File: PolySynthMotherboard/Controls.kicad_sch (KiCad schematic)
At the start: 92 parts, among them SW601 ENV1_B, SW602 ENV2_B, SW603 LFO1_B, SW604 LFO2_B, SW605 LFO3_B, SW606 MIX1_B, SW607 MIX2_B, SW608 MENU_B, SW609 FF_B, SW610 HP_B, SW611 HP_B, U204 ILI9341, U501 MCP23S17_SS

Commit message: board layout
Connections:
- net ENCA_L: now also U501.2 (GPB1); no longer U501.1 (GPB0)
- net ENCA_R: now also U501.1 (GPB0); no longer U501.2 (GPB1)
- net ENCB_L: now also U501.4 (GPB3); no longer U501.3 (GPB2)
- net ENCB_R: now also U501.3 (GPB2); no longer U501.4 (GPB3)
- net ENCC_L: now also U501.6 (GPB5); no longer U501.5 (GPB4), U501.7 (GPB6)
- net ENCC_R: now also U501.5 (GPB4); no longer U501.6 (GPB5), U501.8 (GPB7)
- net ENCD_L: now also U501.8 (GPB7)
- net ENCD_R: now also U501.7 (GPB6)
- net ENV1_B: now also U501.28 (GPA7); no longer U501.21 (GPA0)
- net ENV2_B: now also U501.27 (GPA6); no longer U501.22 (GPA1)
- net LFO1_B: now also U501.26 (GPA5); no longer U501.23 (GPA2)
- net LFO2_B: now also U501.25 (GPA4); no longer U501.24 (GPA3)
- net LFO3_B: now also U501.24 (GPA3); no longer U501.25 (GPA4)
- net MENU_B: now also U501.21 (GPA0); no longer U501.28 (GPA7)
- net MIX1_B: now also U501.23 (GPA2); no longer U501.26 (GPA5)
- net MIX2_B: now also U501.22 (GPA1); no longer U501.27 (GPA6)
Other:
- moved on the sheet: R625, R626, SW609, SW610

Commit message: new voice board proj
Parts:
- RE606: value ENC_RES -> ENC_LES
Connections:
- net ENCA_L: now also C217.1, R601.2, RE601.A, U501.1 (GPB0); no longer C217.1, R602.2, RE601.B, U501.2 (GPB1)
- net ENCA_R: now also C217.1, R602.2, RE601.B, U501.2 (GPB1); no longer C217.1, R601.2, RE601.A, U501.1 (GPB0)
- net ENCB_L: now also C217.1, R605.2, RE602.A, U501.3 (GPB2); no longer C217.1, R606.2, RE602.B, U501.4 (GPB3)
- net ENCB_R: now also C217.1, R606.2, RE602.B, U501.4 (GPB3); no longer C217.1, R605.2, RE602.A, U501.3 (GPB2)
- net ENCCF_L: now also C217.1, R617.2, RE605.A, U501.28 (GPA7); no longer C217.1, R618.2, RE605.B, U501.21 (GPA0)
- net ENCCF_R: now also C217.1, R618.2, RE605.B, U501.27 (GPA6); no longer C217.1, R617.2, RE605.A, U501.22 (GPA1)
- net ENCC_L: now also C217.1, R608.2, RE603.A, U501.5 (GPB4); no longer C217.1, R609.2, RE603.B, U501.6 (GPB5)
- net ENCC_R: now also C217.1, R609.2, RE603.B, U501.6 (GPB5); no longer C217.1, R608.2, RE603.A, U501.5 (GPB4)
- net ENCDEPTH_L: now also C217.1, R627.2, RE609.A, U501.8 (GPB7); no longer C217.1, R628.2, RE609.B, U501.7 (GPB6)
- net ENCDEPTH_R: now also C217.1, R628.2, RE609.B, U501.7 (GPB6); no longer C217.1, R627.2, RE609.A, U501.8 (GPB7)
- net ENCD_L: now also C217.1, R611.2, RE604.A, U501.7 (GPB6); no longer C217.1, R612.2, RE604.B, U501.8 (GPB7)
- net ENCD_R: now also C217.1, R612.2, RE604.B, U501.8 (GPB7); no longer C217.1, R611.2, RE604.A, U501.7 (GPB6)
- net ENCFOLD_L: now also C217.1, R623.2, RE608.A, U501.22 (GPA1); no longer C217.1, R624.2, RE608.B, U501.27 (GPA6)
- net ENCFOLD_R: now also C217.1, R624.2, RE608.B, U501.21 (GPA0); no longer C217.1, R623.2, RE608.A, U501.28 (GPA7)
- net ENCPWM_L: now also C217.1, R621.2, RE607.A, U501.24 (GPA3); no longer C217.1, R622.2, RE607.B, U501.25 (GPA4)
- net ENCPWM_R: now also C217.1, R622.2, RE607.B, U501.23 (GPA2); no longer C217.1, R621.2, RE607.A, U501.26 (GPA5)
- net ENCRES_L: now also C217.1, R619.2, RE606.A, U501.26 (GPA5); no longer C217.1, R620.2, RE606.B, U501.23 (GPA2)
- net ENCRES_R: now also C217.1, R620.2, RE606.B, U501.25 (GPA4); no longer C217.1, R619.2, RE606.A, U501.24 (GPA3)
- net DISP_RST renamed DISP_LST

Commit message: fixed git maybe
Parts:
- added C217 (x2): 10n, Capacitor_SMD:C_0805_2012Metric, symbol Device:C
- added R630, R631, R632: 47k, PCM_Resistor_SMD_AKL:R_0805_2012Metric, symbol Device:R_US
- added SW612: ENC_MENU, Alps_Rotary_Encoder:RotaryEncoder_Alps_EC11E-Switch_Vertical_H20mm_5Pin, symbol Device:RotaryEncoder_Switch
- SW608: value MENU_B -> ALT_B
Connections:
- net +3.3V: now also R630.1, R631.1, R632.1
- net GND: now also C217.2, C217.2, SW612.C, SW612.S2
- net MENU_B: now also U501.1 (GPB0), R632.2, SW612.S1; no longer R616.2, SW608.2 (B), U501.21 (GPA0)
- net ENCMENU_R: now reaches U501.2 (GPB1)
- net ENCMENU_R: now also C217.1, R631.2, SW612.B
- net ENCMENU_L: now reaches U501.3 (GPB2)
- net ENCMENU_L: now also C217.1, R630.2, SW612.A
- new net ALT_B: R616.2, SW608.2 (B), U501.21 (GPA0)
- no-connect marks 5 -> 2
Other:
- moved on the sheet: C217, R616, SW608, U204

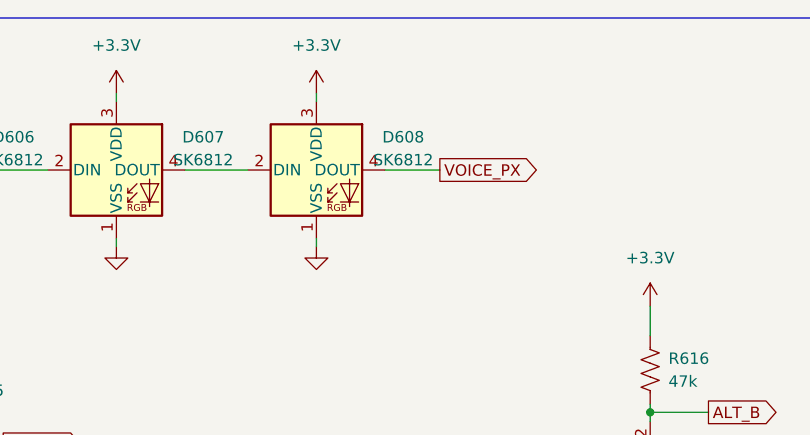
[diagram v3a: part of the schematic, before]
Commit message: cleaned up CV opamps
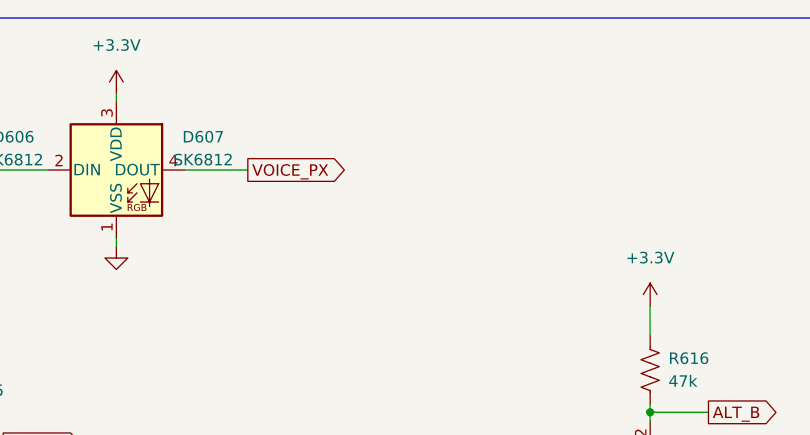
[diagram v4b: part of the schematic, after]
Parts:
- removed D608: SK6812, LED_SMD:LED_SK6812_PLCC4_5.0x5.0mm_P3.2mm, symbol LED:SK6812
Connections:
- net VOICE_PX: now also D607.4 (DOUT)
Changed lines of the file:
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@@
     (stroke (width 0) (type default))
   )
-  (wire (pts (xy 197.104 33.274) (xy 203.2 33.274))
-    (stroke (width 0) (type default))
-  )
   (wire (pts (xy 149.098 231.14) (xy 149.098 232.156))
     (stroke (width 0) (type default))
@@
     (stroke (width 0) (type default))
   )
-  (wire (pts (xy 189.484 40.894) (xy 189.484 41.783))
-    (stroke (width 0) (type default))
-  )
   (wire (pts (xy 225.679 116.332) (xy 225.679 117.602))
     (stroke (width 0) (type default))
@@
     (stroke (width 0) (type default))
   )
-  (wire (pts (xy 189.484 24.765) (xy 189.484 25.654))
-    (stroke (width 0) (type default))
-  )
   (wire (pts (xy 156.845 219.075) (xy 156.845 220.345))
     (stroke (width 0) (type default))
@@
     )
   )
-  (global_label "VOICE_PX" (shape output) (at 203.2 33.274 0) (fields_autoplaced)
+  (global_label "VOICE_PX" (shape output) (at 181.864 33.274 0) (fields_autoplaced)
     (effects (font (size 1.27 1.27)) (justify left))
-    (property "Intersheetrefs" "${INTERSHEET_REFS}" (at 215.0752 33.274 0)
+    (property "Intersheetrefs" "${INTERSHEET_REFS}" (at 193.7392 33.274 0)
       (effects (font (size 1.27 1.27)) (justify left) hide)
     )
@@
     )
   )
-  (symbol (lib_id "LED:SK6812") (at 189.484 33.274 0) (unit 1)
-    (in_bom yes) (on_board yes) (dnp no) (fields_autoplaced)
-    (property "Reference" "D608" (at 199.136 29.6261 0)
-      (effects (font (size 1.27 1.27)))
-    )
-    (property "Value" "SK6812" (at 199.136 32.1661 0)
-      (effects (font (size 1.27 1.27)))
-    )
-    (property "Footprint" "LED_SMD:LED_SK6812_PLCC4_5.0x5.0mm_P3.2mm" (at 190.754 40.894 0)
-      (effects (font (size 1.27 1.27)) (justify left top) hide)
-    )
-    (property "Datasheet" "https://cdn-shop.adafruit.com/product-files/1138/SK6812+LED+datasheet+.pdf" (at 192.024 42.799 0)
-      (effects (font (size 1.27 1.27)) (justify left top) hide)
-    )
-    (pin "1")
-    (pin "2")
-    (pin "3")
-    (pin "4")
-    (instances
-      (project "PolySynthMotherboard"
-        (path "/22649217-9810-470f-bc7b-6f743ad2b90e/f0372297-a883-4012-af0b-9ec6adb58eca"
-          (reference "D608") (unit 1)
-        )
-      )
-    )
-  )
   (symbol (lib_id "Device:C") (at 365.633 36.449 0) (unit 1)
     (in_bom yes) (on_board yes) (dnp no)
@@
     )
   )
-  (symbol (lib_id "power:+3.3V") (at 189.484 24.765 0) (unit 1)
-    (in_bom yes) (on_board yes) (dnp no) (fields_autoplaced)
-    (property "Reference" "#PWR0695" (at 189.484 28.575 0)
-      (effects (font (size 1.27 1.27)) hide)
-    )
-    (property "Value" "+3.3V" (at 189.484 19.431 0)
-      (effects (font (size 1.27 1.27)))
-    )
-    (property "Footprint" "" (at 189.484 24.765 0)
-      (effects (font (size 1.27 1.27)) hide)
-    )
-    (property "Datasheet" "" (at 189.484 24.765 0)
-      (effects (font (size 1.27 1.27)) hide)
-    )
-    (pin "1")
-    (instances
-      (project "PolySynthMotherboard"
-        (path "/22649217-9810-470f-bc7b-6f743ad2b90e/f0372297-a883-4012-af0b-9ec6adb58eca"
-          (reference "#PWR0695") (unit 1)
-        )
-      )
-    )
-  )
   (symbol (lib_id "Device:R_US") (at 180.721 154.178 0) (unit 1)
     (in_bom yes) (on_board yes) (dnp no) (fields_autoplaced)
@@
         )
       )
-    )
-  )
-  (symbol (lib_id "power:GND") (at 189.484 41.783 0) (unit 1)
-    (in_bom yes) (on_board yes) (dnp no) (fields_autoplaced)
-    (property "Reference" "#PWR0696" (at 189.484 48.133 0)
-      (effects (font (size 1.27 1.27)) hide)
-    )
-    (property "Value" "GND" (at 189.484 45.593 0)
-      (effects (font (size 1.27 1.27)) hide)
-    )
-    (property "Footprint" "" (at 189.484 41.783 0)
-      (effects (font (size 1.27 1.27)) hide)
-    )
-    (property "Datasheet" "" (at 189.484 41.783 0)
-      (effects (font (size 1.27 1.27)) hide)
-    )
-    (pin "1")
-    (instances
-      (project "PolySynthMotherboard"
-        (path "/22649217-9810-470f-bc7b-6f743ad2b90e/f0372297-a883-4012-af0b-9ec6adb58eca"
-          (reference "#PWR0696") (unit 1)
-        )
-      )

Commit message: footprints placed
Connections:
- net ALT_B: now also U501.28 (GPA7); no longer U501.21 (GPA0)
- net ENCA_L: now also U501.8 (GPB7); no longer U501.1 (GPB0)
- net ENCA_R: now also U501.7 (GPB6); no longer U501.2 (GPB1)
- net ENCB_L: now also U501.6 (GPB5); no longer U501.3 (GPB2)
- net ENCB_R: now also U501.5 (GPB4); no longer U501.4 (GPB3)
- net ENCC_L: now also U501.4 (GPB3); no longer U501.5 (GPB4)
- net ENCC_R: now also U501.3 (GPB2); no longer U501.6 (GPB5)
- net ENCD_L: now also U501.2 (GPB1); no longer U501.7 (GPB6)
- net ENCD_R: now also U501.1 (GPB0); no longer U501.8 (GPB7)
- net ENV1_B: now also U501.21 (GPA0); no longer U501.28 (GPA7)
- net ENV2_B: now also U501.22 (GPA1); no longer U501.27 (GPA6)
- net LFO1_B: now also U501.23 (GPA2); no longer U501.26 (GPA5)
- net LFO2_B: now also U501.24 (GPA3); no longer U501.25 (GPA4)
- net LFO3_B: now also U501.25 (GPA4); no longer U501.24 (GPA3)
- net MIX1_B: now also U501.26 (GPA5); no longer U501.23 (GPA2)
- net MIX2_B: now also U501.27 (GPA6); no longer U501.22 (GPA1)
- net DISP_LST renamed DISP_RST
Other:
- moved on the sheet: C217, C501, R616, R630, R631, R632, SW608, SW612, U204, U501

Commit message: motherboard rev1
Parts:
- added TP706: EXP_SCK, TestPoint:TestPoint_Pad_D1.0mm_Value, symbol Connector:TestPoint
- added TP706: EXP_MISO, TestPoint:TestPoint_Pad_D1.0mm_Value, symbol Connector:TestPoint
- added TP706: EXP_MOSI, TestPoint:TestPoint_Pad_D1.0mm_Value, symbol Connector:TestPoint
- added TP706: EXP_CS, TestPoint:TestPoint_Pad_D1.0mm_Value, symbol Connector:TestPoint
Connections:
- net FFMODE_B is gone; now on net FF_B: U501.6 (GPB5)
- net ALT_B: now also U501.21 (GPA0); no longer U501.28 (GPA7)
- net ENV1_B: now also U501.22 (GPA1); no longer U501.21 (GPA0)
- net ENV2_B: now also U501.23 (GPA2); no longer U501.22 (GPA1)
- net EXP_CS: now also TP706.1
- net EXP_INTR_B: now also U501.19 (INTB); no longer U501.19 (INTB)
- net EXP_INTR_C: now also U501.19 (INTB); no longer U501.19 (INTB)
- net EXP_MISO: now also TP706.1
- net EXP_MOSI: now also TP706.1
- net EXP_SCK: now also TP706.1
- net LFO1_B: now also U501.24 (GPA3); no longer U501.23 (GPA2)
- net LFO2_B: now also U501.25 (GPA4); no longer U501.24 (GPA3)
- net LFO3_B: now also U501.26 (GPA5); no longer U501.25 (GPA4)
- net MIX1_B: now also U501.27 (GPA6); no longer U501.26 (GPA5)
- net MIX2_B: now also U501.28 (GPA7); no longer U501.27 (GPA6)
